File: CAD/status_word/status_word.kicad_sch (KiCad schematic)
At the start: 47 parts, among them J1 Conn_01x26_Pin, U1 74HC161, U2 74HC109, U3 74HC157, U4 74HC157, U5 74HC245, U6 74HC02

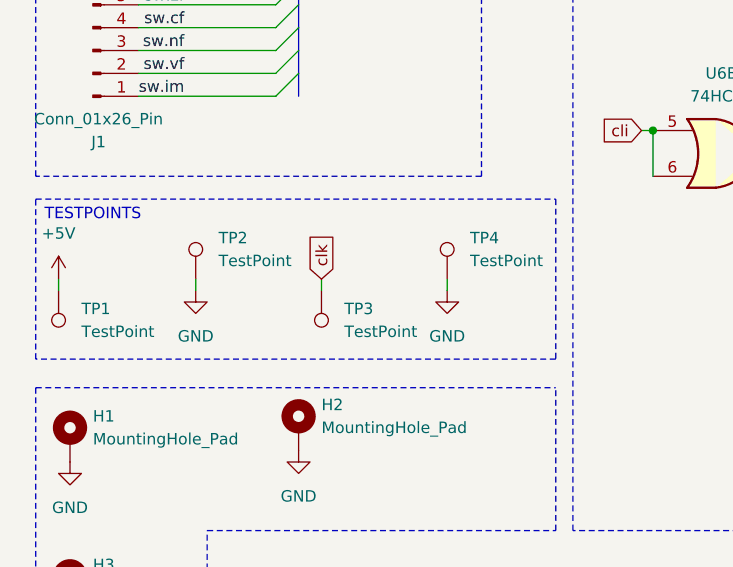
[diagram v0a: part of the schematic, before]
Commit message: SW add keystone 5015 testpoint, small layout improvements
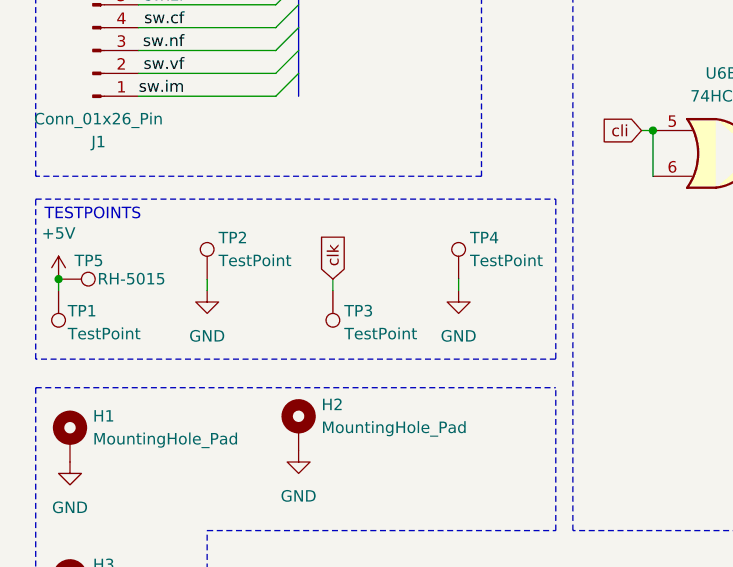
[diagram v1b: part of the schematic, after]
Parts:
- added TP5: RH-5015, TestPoint:TestPoint_Keystone_5015_Micro_Mini, symbol Connector:TestPoint
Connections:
- net +5V: now also TP5.1
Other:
- moved on the sheet: TP2, TP3, TP4

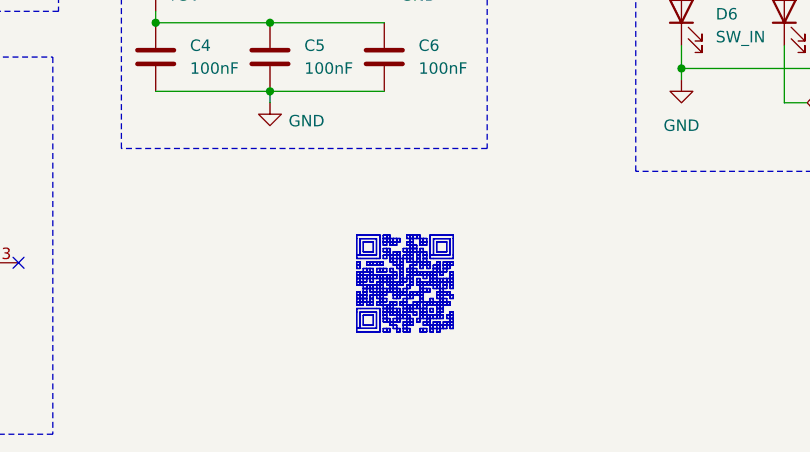
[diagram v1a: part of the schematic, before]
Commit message: update KiCAD version 10.0
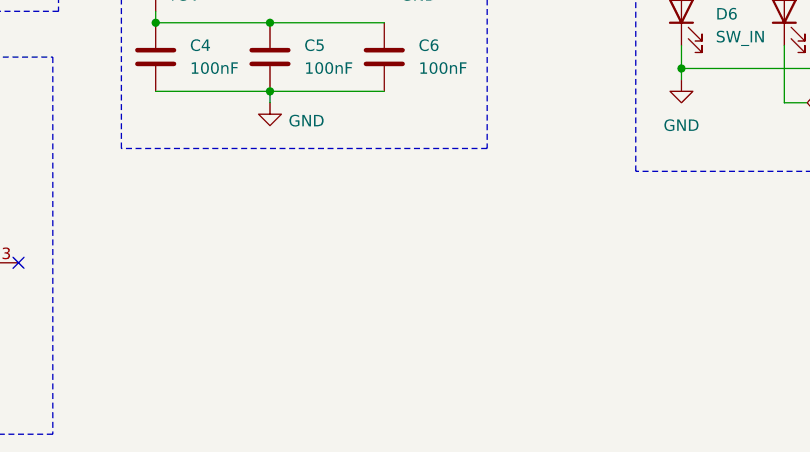
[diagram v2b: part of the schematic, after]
